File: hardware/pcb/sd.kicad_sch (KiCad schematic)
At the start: 17 parts, among them J6 Micro_SD_Card_Det1, J7 Micro_SD_Card_Det1

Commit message: added pullups for jtag
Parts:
- renumbered R37 to R43, R39 to R44, R41 to R45, R43 to R46, R45 to R47, R47 to R48, R38 to R49, R40 to R50, R42 to R51, R44 to R52, R46 to R53, R48 to R54
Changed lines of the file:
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@@
 		(in_pos_files yes)
 		(dnp no)
-		(property "Reference" "R45"
+		(property "Reference" "R47"
 			(at 86.868 36.195 0)
 			(show_name no)
@@
 			(project "meko"
 				(path "/da54f10a-146b-4941-a9c7-55c7173bb101/45aa24d2-e0af-4ebb-a68a-61b6a12c0eec"
-					(reference "R45")
+					(reference "R47")
 					(unit 1)
 				)
@@
 		(in_pos_files yes)
 		(dnp no)
-		(property "Reference" "R37"
+		(property "Reference" "R43"
 			(at 61.468 36.195 0)
 			(show_name no)
@@
 			(project "meko"
 				(path "/da54f10a-146b-4941-a9c7-55c7173bb101/45aa24d2-e0af-4ebb-a68a-61b6a12c0eec"
-					(reference "R37")
+					(reference "R43")
 					(unit 1)
 				)
@@
 		(in_pos_files yes)
 		(dnp no)
-		(property "Reference" "#PWR0119"
+		(property "Reference" "#PWR0120"
 			(at 102.87 55.88 0)
 			(hide yes)
@@
 			(project "meko"
 				(path "/da54f10a-146b-4941-a9c7-55c7173bb101/45aa24d2-e0af-4ebb-a68a-61b6a12c0eec"
-					(reference "#PWR0119")
+					(reference "#PWR0120")
 					(unit 1)
 				)
@@
 		(in_pos_files yes)
 		(dnp no)
-		(property "Reference" "R38"
+		(property "Reference" "R49"
 			(at 61.468 104.775 0)
 			(show_name no)
@@
 			(project "meko"
 				(path "/da54f10a-146b-4941-a9c7-55c7173bb101/45aa24d2-e0af-4ebb-a68a-61b6a12c0eec"
-					(reference "R38")
+					(reference "R49")
 					(unit 1)
 				)
@@
 		(in_pos_files yes)
 		(dnp no)
-		(property "Reference" "#PWR0128"
+		(property "Reference" "#PWR0127"
 			(at 153.67 134.62 0)
 			(hide yes)
@@
 			(project "meko"
 				(path "/da54f10a-146b-4941-a9c7-55c7173bb101/45aa24d2-e0af-4ebb-a68a-61b6a12c0eec"
-					(reference "#PWR0128")
+					(reference "#PWR0127")
 					(unit 1)
 				)
@@
 		(in_pos_files yes)
 		(dnp no)
-		(property "Reference" "R44"
+		(property "Reference" "R52"
 			(at 80.518 104.775 0)
 			(show_name no)
@@
 			(project "meko"
 				(path "/da54f10a-146b-4941-a9c7-55c7173bb101/45aa24d2-e0af-4ebb-a68a-61b6a12c0eec"
-					(reference "R44")
+					(reference "R52")
 					(unit 1)
 				)
@@
 		(in_pos_files yes)
 		(dnp no)
-		(property "Reference" "#PWR0117"
+		(property "Reference" "#PWR0118"
 			(at 58.42 34.29 0)
 			(hide yes)
@@
 			(project "meko"
 				(path "/da54f10a-146b-4941-a9c7-55c7173bb101/45aa24d2-e0af-4ebb-a68a-61b6a12c0eec"
-					(reference "#PWR0117")
+					(reference "#PWR0118")
 					(unit 1)
 				)
@@
 		(in_pos_files yes)
 		(dnp no)
-		(property "Reference" "R46"
+		(property "Reference" "R53"
 			(at 86.868 104.775 0)
 			(show_name no)
@@
 			(project "meko"
 				(path "/da54f10a-146b-4941-a9c7-55c7173bb101/45aa24d2-e0af-4ebb-a68a-61b6a12c0eec"
-					(reference "R46")
+					(reference "R53")
 					(unit 1)
 				)
@@
 		(in_pos_files yes)
 		(dnp no)
-		(property "Reference" "R47"
+		(property "Reference" "R48"
 			(at 93.218 36.195 0)
 			(show_name no)
@@
 			(project "meko"
 				(path "/da54f10a-146b-4941-a9c7-55c7173bb101/45aa24d2-e0af-4ebb-a68a-61b6a12c0eec"
-					(reference "R47")
+					(reference "R48")
 					(unit 1)
 				)
@@
 		(in_pos_files yes)
 		(dnp no)
-		(property "Reference" "R40"
+		(property "Reference" "R50"
 			(at 67.818 104.775 0)
 			(show_name no)
@@
 			(project "meko"
 				(path "/da54f10a-146b-4941-a9c7-55c7173bb101/45aa24d2-e0af-4ebb-a68a-61b6a12c0eec"
-					(reference "R40")
+					(reference "R50")
 					(unit 1)
 				)
@@
 		(in_pos_files yes)
 		(dnp no)
-		(property "Reference" "R42"
+		(property "Reference" "R51"
 			(at 74.168 104.775 0)
 			(show_name no)
@@
 			(project "meko"
 				(path "/da54f10a-146b-4941-a9c7-55c7173bb101/45aa24d2-e0af-4ebb-a68a-61b6a12c0eec"
-					(reference "R42")
+					(reference "R51")
 					(unit 1)
 				)
@@
 		(in_pos_files yes)
 		(dnp no)
-		(property "Reference" "#PWR0121"
+		(property "Reference" "#PWR0126"
 			(at 102.87 124.46 0)
 			(hide yes)
@@
 			(project "meko"
 				(path "/da54f10a-146b-4941-a9c7-55c7173bb101/45aa24d2-e0af-4ebb-a68a-61b6a12c0eec"
-					(reference "#PWR0121")
+					(reference "#PWR0126")
 					(unit 1)
 				)
@@
 		(in_pos_files yes)
 		(dnp no)
-		(property "Reference" "#PWR0120"
+		(property "Reference" "#PWR0122"
 			(at 92.71 60.96 0)
 			(hide yes)
@@
 			(project "meko"
 				(path "/da54f10a-146b-4941-a9c7-55c7173bb101/45aa24d2-e0af-4ebb-a68a-61b6a12c0eec"
-					(reference "#PWR0120")
+					(reference "#PWR0122")
 					(unit 1)
 				)
@@
 		(in_pos_files yes)
 		(dnp no)
-		(property "Reference" "#PWR0127"
+		(property "Reference" "#PWR0125"
 			(at 153.67 124.46 0)
 			(hide yes)
@@
 			(project "meko"
 				(path "/da54f10a-146b-4941-a9c7-55c7173bb101/45aa24d2-e0af-4ebb-a68a-61b6a12c0eec"
-					(reference "#PWR0127")
+					(reference "#PWR0125")
 					(unit 1)
 				)
@@
 		(in_pos_files yes)
 		(dnp no)
-		(property "Reference" "#PWR0122"
+		(property "Reference" "#PWR0128"
 			(at 92.71 129.54 0)
 			(hide yes)
@@
 			(project "meko"
 				(path "/da54f10a-146b-4941-a9c7-55c7173bb101/45aa24d2-e0af-4ebb-a68a-61b6a12c0eec"
-					(reference "#PWR0122")
+					(reference "#PWR0128")
 					(unit 1)
 				)
@@
 		(in_pos_files yes)
 		(dnp no)
-		(property "Reference" "#PWR0125"
+		(property "Reference" "#PWR0119"
 			(at 153.67 55.88 0)
 			(hide yes)
@@
 			(project "meko"
 				(path "/da54f10a-146b-4941-a9c7-55c7173bb101/45aa24d2-e0af-4ebb-a68a-61b6a12c0eec"
-					(reference "#PWR0125")
+					(reference "#PWR0119")
 					(unit 1)
 				)
@@
 		(in_pos_files yes)
 		(dnp no)
-		(property "Reference" "#PWR0126"
+		(property "Reference" "#PWR0121"
 			(at 153.67 66.04 0)
 			(hide yes)
@@
 			(project "meko"
 				(path "/da54f10a-146b-4941-a9c7-55c7173bb101/45aa24d2-e0af-4ebb-a68a-61b6a12c0eec"
-					(reference "#PWR0126")
+					(reference "#PWR0121")
 					(unit 1)
 				)
@@
 		(in_pos_files yes)
 		(dnp no)
-		(property "Reference" "R39"
+		(property "Reference" "R44"
 			(at 67.818 36.195 0)
 			(show_name no)
@@
 			(project "meko"
 				(path "/da54f10a-146b-4941-a9c7-55c7173bb101/45aa24d2-e0af-4ebb-a68a-61b6a12c0eec"
-					(reference "R39")
+					(reference "R44")
 					(unit 1)
 				)
@@
 		(in_pos_files yes)
 		(dnp no)
-		(property "Reference" "R41"
+		(property "Reference" "R45"
 			(at 74.168 36.195 0)
 			(show_name no)
@@
 			(project "meko"
 				(path "/da54f10a-146b-4941-a9c7-55c7173bb101/45aa24d2-e0af-4ebb-a68a-61b6a12c0eec"
-					(reference "R41")
+					(reference "R45")
 					(unit 1)
 				)
@@
 		(in_pos_files yes)
 		(dnp no)
-		(property "Reference" "#PWR0124"
+		(property "Reference" "#PWR0129"
 			(at 144.78 147.32 0)
 			(hide yes)
@@
 			(project "meko"
 				(path "/da54f10a-146b-4941-a9c7-55c7173bb101/45aa24d2-e0af-4ebb-a68a-61b6a12c0eec"
-					(reference "#PWR0124")
+					(reference "#PWR0129")
 					(unit 1)
 				)
@@
 		(in_pos_files yes)
 		(dnp no)
-		(property "Reference" "R43"
+		(property "Reference" "R46"
 			(at 80.518 36.195 0)
 			(show_name no)
@@
 			(project "meko"
 				(path "/da54f10a-146b-4941-a9c7-55c7173bb101/45aa24d2-e0af-4ebb-a68a-61b6a12c0eec"
-					(reference "R43")
+					(reference "R46")
 					(unit 1)
 				)
@@
 		(in_pos_files yes)
 		(dnp no)
-		(property "Reference" "R48"
+		(property "Reference" "R54"
 			(at 93.218 104.775 0)
 			(show_name no)
@@
 			(project "meko"
 				(path "/da54f10a-146b-4941-a9c7-55c7173bb101/45aa24d2-e0af-4ebb-a68a-61b6a12c0eec"
-					(reference "R48")
+					(reference "R54")
 					(unit 1)
 				)
@@
 		(in_pos_files yes)
 		(dnp no)
-		(property "Reference" "#PWR0118"
+		(property "Reference" "#PWR0124"
 			(at 58.42 102.87 0)
 			(hide yes)
@@
 			(project "meko"
 				(path "/da54f10a-146b-4941-a9c7-55c7173bb101/45aa24d2-e0af-4ebb-a68a-61b6a12c0eec"
-					(reference "#PWR0118")
-					(unit 1)
-				)
+					(reference "#PWR0124")
+					(unit 1)
+				)

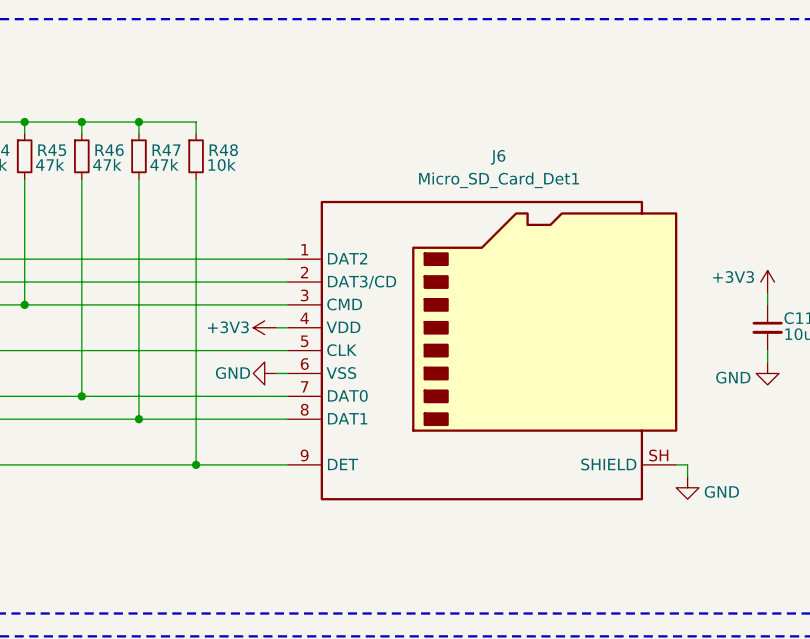
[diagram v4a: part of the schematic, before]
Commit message: fixed small issues with footprint pad names
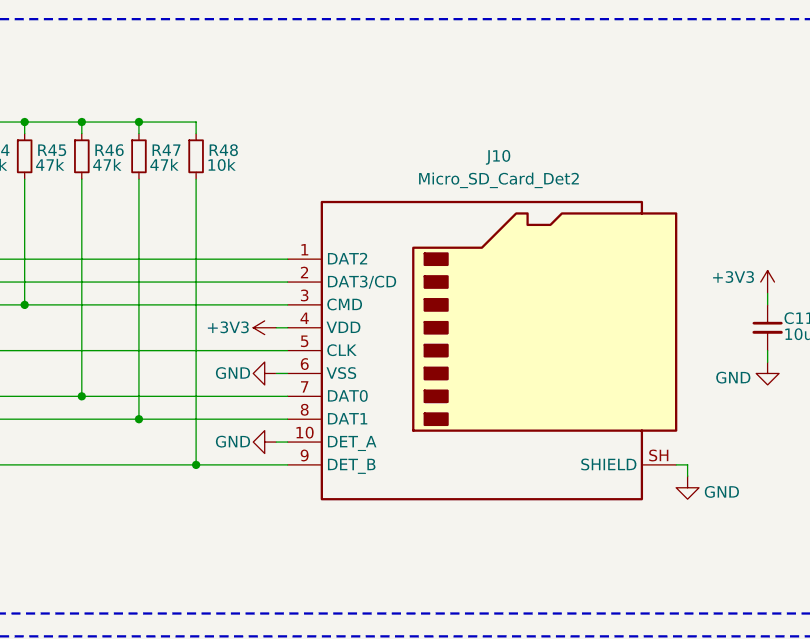
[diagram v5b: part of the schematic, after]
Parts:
- removed J6: Micro_SD_Card_Det1, PCM_ckl-connector:microSD_SOFNG_TF-008, symbol Connector:Micro_SD_Card_Det1
- added J10: Micro_SD_Card_Det2, PCM_ckl-connector:microSD_SOFNG_TF-008, symbol Connector:Micro_SD_Card_Det2
- J7: LCSC (none) -> C20613194; MPN (none) -> TF-015-ZYD9AH1.85
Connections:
- net +3V3: now also J10.4 (VDD)
- net BOOT.CD: now also J10.9 (DET_B)
- net BOOT.CK: now also J10.5 (CLK)
- net BOOT.CMD: now also J10.3 (CMD)
- net BOOT.DAT0: now also J10.7 (DAT0)
- net BOOT.DAT1: now also J10.8 (DAT1)
- net BOOT.DAT2: now also J10.1 (DAT2)
- net BOOT.DAT3: now also J10.2 (DAT3/CD)
- net GND: now also J10.10 (DET_A), J10.6 (VSS), J10.SH (SHIELD)
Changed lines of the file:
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@@
+	(wire
+		(pts
+			(xy 99.06 68.58) (xy 100.33 68.58)
+		)
+		(stroke
+			(width 0)
+			(type default)
+		)
+	)
 	(wire
 		(pts
@@
 			)
 		)
-		(property "Datasheet" "https://datasheet.lcsc.com/lcsc/2110151630_XKB-Connectivity-XKTF-015-N_C381082.pdf"
+		(property "Datasheet" "https://www.lcsc.com/datasheet/C20613194.pdf"
 			(at 123.19 124.46 0)
 			(hide yes)
@@
 			)
 		)
-		(property "KLC_S3.3" ""
+		(property "MPN" "TF-015-ZYD9AH1.85"
 			(at 123.19 127 0)
 			(hide yes)
@@
 			)
 		)
-		(property "KLC_S4.1" ""
+		(property "LCSC" "C20613194"
 			(at 123.19 127 0)
 			(hide yes)
@@
 				(path "/da54f10a-146b-4941-a9c7-55c7173bb101/45aa24d2-e0af-4ebb-a68a-61b6a12c0eec"
 					(reference "#PWR0127")
-					(unit 1)
-				)
-			)
-		)
-	)
-	(symbol
-		(lib_id "Connector:Micro_SD_Card_Det1")
-		(at 123.19 58.42 0)
-		(unit 1)
-		(body_style 1)
-		(exclude_from_sim no)
-		(in_bom yes)
-		(on_board yes)
-		(in_pos_files yes)
-		(dnp no)
-		(fields_autoplaced yes)
-		(property "Reference" "J6"
-			(at 123.825 36.83 0)
-			(show_name no)
-			(do_not_autoplace no)
-			(effects
-				(font
-					(size 1.27 1.27)
-				)
-			)
-		)
-		(property "Value" "Micro_SD_Card_Det1"
-			(at 123.825 39.37 0)
-			(show_name no)
-			(do_not_autoplace no)
-			(effects
-				(font
-					(size 1.27 1.27)
-				)
-			)
-		)
-		(property "Footprint" "PCM_ckl-connector:microSD_SOFNG_TF-008"
-			(at 175.26 40.64 0)
-			(hide yes)
-			(show_name no)
-			(do_not_autoplace no)
-			(effects
-				(font
-					(size 1.27 1.27)
-				)
-			)
-		)
-		(property "Datasheet" "https://datasheet.lcsc.com/lcsc/2110151630_XKB-Connectivity-XKTF-015-N_C381082.pdf"
-			(at 123.19 55.88 0)
-			(hide yes)
-			(show_name no)
-			(do_not_autoplace no)
-			(effects
-				(font
-					(size 1.27 1.27)
-				)
-			)
-		)
-		(property "Description" "Micro SD Card Socket with one card detection pin"
-			(at 123.19 58.42 0)
-			(hide yes)
-			(show_name no)
-			(do_not_autoplace no)
-			(effects
-				(font
-					(size 1.27 1.27)
-				)
-			)
-		)
-		(property "KLC_S3.3" ""
-			(at 123.19 58.42 0)
-			(hide yes)
-			(show_name no)
-			(do_not_autoplace no)
-			(effects
-				(font
-					(size 1.27 1.27)
-				)
-			)
-		)
-		(property "KLC_S4.1" ""
-			(at 123.19 58.42 0)
-			(hide yes)
-			(show_name no)
-			(do_not_autoplace no)
-			(effects
-				(font
-					(size 1.27 1.27)
-				)
-			)
-		)
-		(pin "9"
-		)
-		(pin "6"
-		)
-		(pin "3"
-		)
-		(pin "5"
-		)
-		(pin "7"
-		)
-		(pin "1"
-		)
-		(pin "2"
-		)
-		(pin "4"
-		)
-		(pin "8"
-		)
-		(pin "SH"
-		)
-		(instances
-			(project "meko"
-				(path "/da54f10a-146b-4941-a9c7-55c7173bb101/45aa24d2-e0af-4ebb-a68a-61b6a12c0eec"
-					(reference "J6")
 					(unit 1)
 				)
@@
 					(unit 1)
 				)
+			)
+		)
+	)
+	(symbol
+		(lib_id "power:GND")
+		(at 99.06 68.58 270)
+		(unit 1)
+		(body_style 1)
+		(exclude_from_sim no)
+		(in_bom yes)
+		(on_board yes)
+		(in_pos_files yes)
+		(dnp no)
+		(property "Reference" "#PWR0142"
+			(at 92.71 68.58 0)
+			(hide yes)
+			(show_name no)
+			(do_not_autoplace no)
+			(effects
+				(font
+					(size 1.27 1.27)
+				)
+			)
+		)
+		(property "Value" "GND"
+			(at 96.266 68.58 90)
+			(show_name no)
+			(do_not_autoplace no)
+			(effects
+				(font
+					(size 1.27 1.27)
+				)
+				(justify right)
+			)
+		)
+		(property "Footprint" ""
+			(at 99.06 68.58 0)
+			(hide yes)
+			(show_name no)
+			(do_not_autoplace no)
+			(effects
+				(font
+					(size 1.27 1.27)
+				)
+			)
+		)
+		(property "Datasheet" ""
+			(at 99.06 68.58 0)
+			(hide yes)
+			(show_name no)
+			(do_not_autoplace no)
+			(effects
+				(font
+					(size 1.27 1.27)
+				)
+			)
+		)
+		(property "Description" "Power symbol creates a global label with name \"GND\" , ground"
+			(at 99.06 68.58 0)
+			(hide yes)
+			(show_name no)
+			(do_not_autoplace no)
+			(effects
+				(font
+					(size 1.27 1.27)
+				)
+			)
+		)
+		(pin "1"
+		)
+		(instances
+			(project "meko"
+				(path "/da54f10a-146b-4941-a9c7-55c7173bb101/45aa24d2-e0af-4ebb-a68a-61b6a12c0eec"
+					(reference "#PWR0142")
+					(unit 1)
+				)
+			)
+		)
+	)
+	(symbol
+		(lib_id "Connector:Micro_SD_Card_Det2")
+		(at 123.19 58.42 0)
+		(unit 1)
+		(body_style 1)
+		(exclude_from_sim no)
+		(in_bom yes)
+		(on_board yes)
+		(in_pos_files yes)
+		(dnp no)
+		(fields_autoplaced yes)
+		(property "Reference" "J10"
+			(at 123.825 36.83 0)
+			(show_name no)
+			(do_not_autoplace no)
+			(effects
+				(font
+					(size 1.27 1.27)
+				)
+			)
+		)
+		(property "Value" "Micro_SD_Card_Det2"
+			(at 123.825 39.37 0)
+			(show_name no)
+			(do_not_autoplace no)
+			(effects
+				(font
+					(size 1.27 1.27)
+				)
+			)
+		)
+		(property "Footprint" "PCM_ckl-connector:microSD_SOFNG_TF-008"
+			(at 175.26 40.64 0)
+			(hide yes)
+			(show_name no)
+			(do_not_autoplace no)
+			(effects
+				(font
+					(size 1.27 1.27)
+				)
+			)
+		)
+		(property "Datasheet" "https://www.lcsc.com/datasheet/C428465.pdf"
+			(at 125.73 55.88 0)
+			(hide yes)
+			(show_name no)
+			(do_not_autoplace no)
+			(effects
+				(font
+					(size 1.27 1.27)
+				)
+			)
+		)
+		(property "Description" "Micro SD Card Socket with two card detection pins"
+			(at 123.19 58.42 0)
+			(hide yes)
+			(show_name no)
+			(do_not_autoplace no)
+			(effects
+				(font
+					(size 1.27 1.27)
+				)
+			)
+		)
+		(property "MPN" "TF-008"
+			(at 123.19 58.42 0)
+			(hide yes)
+			(show_name no)
+			(do_not_autoplace no)
+			(effects
+				(font
+					(size 1.27 1.27)
+				)
+			)
+		)
+		(property "LCSC" "C428465"
+			(at 123.19 58.42 0)
+			(hide yes)
+			(show_name no)
+			(do_not_autoplace no)
+			(effects
+				(font
+					(size 1.27 1.27)
+				)
+			)
+		)
+		(pin "6"
+		)
+		(pin "7"
+		)
+		(pin "9"
+		)
+		(pin "5"
+		)
+		(pin "SH"
+		)
+		(pin "10"
+		)
+		(pin "8"
+		)
+		(pin "1"
+		)
+		(pin "2"
+		)
+		(pin "3"
+		)
+		(pin "4"
+		)
+		(instances
+			(project "meko"
+				(path "/da54f10a-146b-4941-a9c7-55c7173bb101/45aa24d2-e0af-4ebb-a68a-61b6a12c0eec"
+					(reference "J10")
+					(unit 1)
+				)

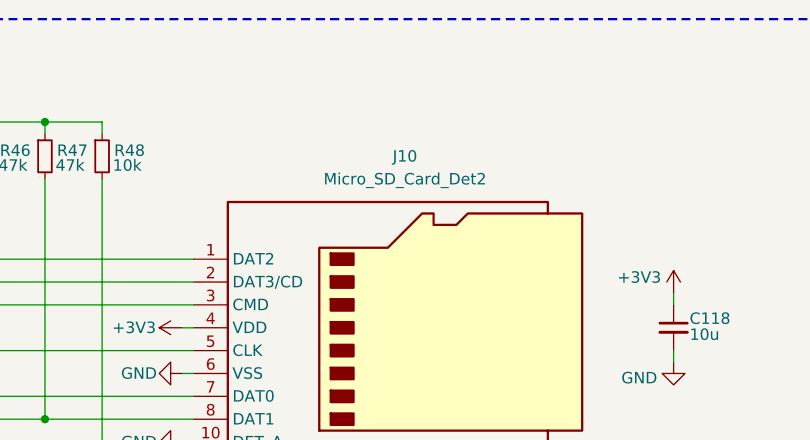
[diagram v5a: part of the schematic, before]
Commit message: moved some caps to 0201
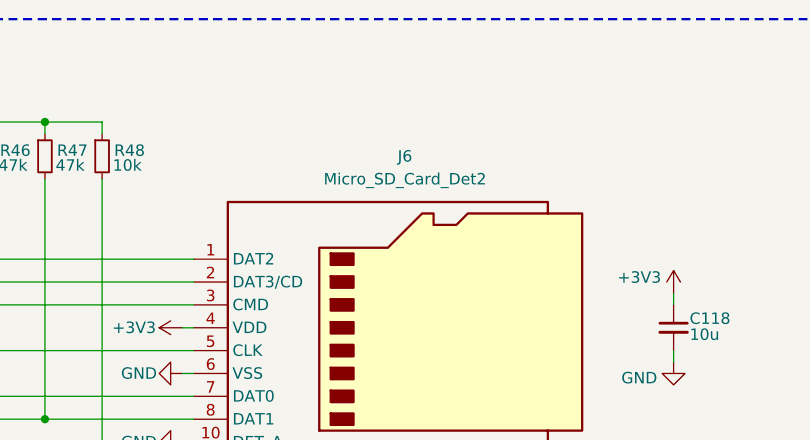
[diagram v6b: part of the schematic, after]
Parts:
- renumbered J10 to J6
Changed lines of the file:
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@@
 		(in_pos_files yes)
 		(dnp no)
-		(property "Reference" "#PWR0127"
+		(property "Reference" "#PWR0128"
 			(at 153.67 134.62 0)
 			(hide yes)
@@
 			(project "meko"
 				(path "/da54f10a-146b-4941-a9c7-55c7173bb101/45aa24d2-e0af-4ebb-a68a-61b6a12c0eec"
-					(reference "#PWR0127")
+					(reference "#PWR0128")
 					(unit 1)
 				)
@@
 		(in_pos_files yes)
 		(dnp no)
-		(property "Reference" "#PWR0126"
+		(property "Reference" "#PWR0127"
 			(at 102.87 124.46 0)
 			(hide yes)
@@
 			(project "meko"
 				(path "/da54f10a-146b-4941-a9c7-55c7173bb101/45aa24d2-e0af-4ebb-a68a-61b6a12c0eec"
-					(reference "#PWR0126")
+					(reference "#PWR0127")
 					(unit 1)
 				)
@@
 		(in_pos_files yes)
 		(dnp no)
-		(property "Reference" "#PWR0125"
+		(property "Reference" "#PWR0126"
 			(at 153.67 124.46 0)
 			(hide yes)
@@
 			(project "meko"
 				(path "/da54f10a-146b-4941-a9c7-55c7173bb101/45aa24d2-e0af-4ebb-a68a-61b6a12c0eec"
-					(reference "#PWR0125")
+					(reference "#PWR0126")
 					(unit 1)
 				)
@@
 		(in_pos_files yes)
 		(dnp no)
-		(property "Reference" "#PWR0128"
+		(property "Reference" "#PWR0129"
 			(at 92.71 129.54 0)
 			(hide yes)
@@
 			(project "meko"
 				(path "/da54f10a-146b-4941-a9c7-55c7173bb101/45aa24d2-e0af-4ebb-a68a-61b6a12c0eec"
-					(reference "#PWR0128")
+					(reference "#PWR0129")
 					(unit 1)
 				)
@@
 		(in_pos_files yes)
 		(dnp no)
-		(property "Reference" "#PWR0123"
+		(property "Reference" "#PWR0124"
 			(at 144.78 78.74 0)
 			(hide yes)
@@
 			(project "meko"
 				(path "/da54f10a-146b-4941-a9c7-55c7173bb101/45aa24d2-e0af-4ebb-a68a-61b6a12c0eec"
-					(reference "#PWR0123")
+					(reference "#PWR0124")
 					(unit 1)
 				)
@@
 		(in_pos_files yes)
 		(dnp no)
-		(property "Reference" "#PWR0142"
+		(property "Reference" "#PWR0123"
 			(at 92.71 68.58 0)
 			(hide yes)
@@
 			(project "meko"
 				(path "/da54f10a-146b-4941-a9c7-55c7173bb101/45aa24d2-e0af-4ebb-a68a-61b6a12c0eec"
-					(reference "#PWR0142")
+					(reference "#PWR0123")
 					(unit 1)
 				)
@@
 		(dnp no)
 		(fields_autoplaced yes)
-		(property "Reference" "J10"
+		(property "Reference" "J6"
 			(at 123.825 36.83 0)
 			(show_name no)
@@
 			(project "meko"
 				(path "/da54f10a-146b-4941-a9c7-55c7173bb101/45aa24d2-e0af-4ebb-a68a-61b6a12c0eec"
-					(reference "J10")
+					(reference "J6")
 					(unit 1)
 				)
@@
 		(in_pos_files yes)
 		(dnp no)
-		(property "Reference" "#PWR0129"
+		(property "Reference" "#PWR0130"
 			(at 144.78 147.32 0)
 			(hide yes)
@@
 			(project "meko"
 				(path "/da54f10a-146b-4941-a9c7-55c7173bb101/45aa24d2-e0af-4ebb-a68a-61b6a12c0eec"
-					(reference "#PWR0129")
+					(reference "#PWR0130")
 					(unit 1)
 				)
@@
 		(in_pos_files yes)
 		(dnp no)
-		(property "Reference" "#PWR0124"
+		(property "Reference" "#PWR0125"
 			(at 58.42 102.87 0)
 			(hide yes)
@@
 			(project "meko"
 				(path "/da54f10a-146b-4941-a9c7-55c7173bb101/45aa24d2-e0af-4ebb-a68a-61b6a12c0eec"
-					(reference "#PWR0124")
-					(unit 1)
-				)
+					(reference "#PWR0125")
+					(unit 1)
+				)

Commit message: vendored in a bunch of footprints
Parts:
- J6: footprint PCM_ckl-connector:microSD_SOFNG_TF-008 -> ckl:microSD_SOFNG_TF-008
- J7: footprint PCM_ckl-connector:microSD_XYECONN_TF-015-ZYD9AH185 -> ckl:microSD_XYECONN_TF-015-ZYD9AH185
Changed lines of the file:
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@@
 			)
 		)
-		(property "Footprint" "PCM_ckl-connector:microSD_XYECONN_TF-015-ZYD9AH185"
+		(property "Footprint" "ckl:microSD_XYECONN_TF-015-ZYD9AH185"
 			(at 175.26 109.22 0)
 			(hide yes)
@@
 			)
 		)
-		(property "Footprint" "PCM_ckl-connector:microSD_SOFNG_TF-008"
+		(property "Footprint" "ckl:microSD_SOFNG_TF-008"
 			(at 175.26 40.64 0)
 			(hide yes)
